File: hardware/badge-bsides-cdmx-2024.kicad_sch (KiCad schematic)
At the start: 26 parts, among them J1 OLED, Q1 DMG3415U-7, SW1 ON, SW2 RESET, SW3 RESET, SW4 RESET, SW5 RESET, SW6 RESET

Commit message: feat(Hw):Added_LED´s_Buttons
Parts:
- D2: value LED1 -> RED; footprint (none) -> LED_SMD:LED_0805_2012Metric; LCSC# (none) -> C965812; provedor (none) -> LCSC
- D3: value LED2 -> Green; footprint (none) -> LED_SMD:LED_0805_2012Metric; LCSC# (none) -> C965815; provedor (none) -> LCSC
- D4: value LED3 -> Blue; footprint (none) -> LED_SMD:LED_0805_2012Metric; LCSC# (none) -> C205441; provedor (none) -> LCSC
- D5: value LED4 -> Yellow; footprint (none) -> LED_SMD:LED_0805_2012Metric; LCSC# (none) -> C84261; provedor (none) -> LCSC
- D6: footprint (none) -> LED_SMD:LED_0805_2012Metric
- J1: value OLED -> Purple; footprint (none) -> LED_SMD:LED_0805_2012Metric; LCSC# (none) -> C7371915
- R2, R3, R4, R5, R6: value 220R -> 330R; footprint (none) -> Resistor_SMD:R_0805_2012Metric_Pad1.20x1.40mm_HandSolder; LCSC# (none) -> C119075; provedor (none) -> LCSC
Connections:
- net RST: now reaches A1.30 (RUN)
- net RST: now also SW5.2
- no-connect marks 0 -> 19

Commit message: fix(Hw):Changed_raspberry
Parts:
- removed A1: SC0918, bsides:MODULE_SC0918, symbol Raspberry_Pi_Pico_W_SC0918:SC0918
- removed BT1: Battery_Cell, symbol Device:Battery_Cell
- removed D3: Green, LED_SMD:LED_0805_2012Metric, symbol Device:LED_Small
- removed D4: Blue, LED_SMD:LED_0805_2012Metric, symbol Device:LED_Small
- removed D5: Yellow, LED_SMD:LED_0805_2012Metric, symbol Device:LED_Small
- removed D6: LED5, LED_SMD:LED_0805_2012Metric, symbol Device:LED_Small
- removed J1: Purple, LED_SMD:LED_0805_2012Metric, symbol Connector:Conn_01x04_Socket
- removed R3, R4, R5, R6: 330R, Resistor_SMD:R_0805_2012Metric_Pad1.20x1.40mm_HandSolder, symbol Device:R_Small
- removed SW5: RESET, Button_Switch_SMD:SW_SPST_TL3342, symbol Switch:SW_Push
- added C5, C6: .1uF, Capacitor_SMD:C_0603_1608Metric, symbol Device:C_Small
- added C8, C9: 10uF, Capacitor_SMD:C_0603_1608Metric, symbol Device:C_Small
- added F1: 0.5A, Fuse:Fuse_0805_2012Metric, symbol Device:Fuse_Small
- added J2: I2C, Connector_PinHeader_2.54mm:PinHeader_1x04_P2.54mm_Vertical, symbol Connector:Screw_Terminal_01x04
- added J3: UART, Connector_PinHeader_2.54mm:PinHeader_1x05_P2.54mm_Vertical, symbol Connector:Screw_Terminal_01x05
- added J4: Battery, Footprint:BAT-TH_BH-AAA-A1AJ024, symbol Connector:Screw_Terminal_01x02
- added J5: OLED, Connector_PinHeader_2.54mm:PinHeader_1x04_P2.54mm_Vertical, symbol Connector:Screw_Terminal_01x04
- added P1: USB_C_Plug_USB2.0, Footprint:C393939, symbol HunterCat-NFC-rescue:USB_C_Plug_USB2.0-Connector
- added R7, R8: 5k1, Resistor_SMD:R_0603_1608Metric, symbol Device:R_Small
- added R9: 10K, Resistor_SMD:R_0603_1608Metric, symbol Device:R_Small
- added SW7: RESET, Button_Switch_SMD:SW_SPST_TL3342, symbol Switch:SW_Push
- added SW8: GPIO, Button_Switch_SMD:SW_SPST_TL3342, symbol Switch:SW_Push
- added U1: ESP32-C6-WROOM-1U-N4, Footprint:MOD28_ESP32-C6-WROOM-1U_EXP, symbol Minino:ESP32-C6-WROOM-1U-N8
- added U2: AP2112K-3.3, Package_TO_SOT_SMD:SOT-23-5, symbol HunterCat-NFC-rescue:AP2112K-3.3-Regulator_Linear
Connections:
- net +BATT: now also J4.2 (Pin_2)
- net GND: now also C5.1, C6.1, C8.2, C9.2, J2.4 (Pin_4), J3.4 (Pin_4), J4.1 (Pin_1), J5.2 (Pin_2), P1.A1 (GND), P1.A12 (GND), P1.B1 (GND), P1.B12 (GND), P1.S1 (SHIELD), R7.1, R8.1, SW7.1, SW8.1, U1.1 (GND), U1.28 (GND), U1.29 (GND), U1.30 (GND), U1.31 (GND), U1.32 (GND), U1.33 (GND), U1.34 (GND), U1.35 (GND), U1.36 (GND), U1.37 (GND), U2.2 (GND)
- net LED1: now also U1.10 (IO8)
- net SCL: now also J2.2 (Pin_2), J5.3 (Pin_3), U1.7 (IO7)
- net SDA: now also J2.3 (Pin_3), J5.4 (Pin_4), U1.6 (IO6)
- net VBUS: now also F1.2
- net GPIO16 renamed GPIO15
- net GPIO15: now also U1.23 (IO15)
- net GPIO17 renamed GPIO23
- net GPIO23: now also U1.21 (IO23)
- net GPIO18 renamed GPIO22
- net GPIO22: now also U1.20 (IO22)
- net GPIO19 renamed GPIO1
- net GPIO1: now also U1.9 (IO1)
- net VCC: no longer names the net of SW1.2 (B)
- net VCC: now also C8.1, U2.1 (VIN), U2.3 (EN)
- new net: P1.A5 (CC), R7.2
- new net: F1.1, P1.A4 (VBUS), P1.A9 (VBUS), P1.B4 (VBUS), P1.B9 (VBUS)
- new net: P1.B5 (VCONN), R8.2
- new net +3V3: C9.1, J2.1 (Pin_1), J3.1 (Pin_1), J5.1 (Pin_1), R9.2, U1.2 (3V3), U2.5 (VOUT)
- new net BOOT: C6.2, SW8.2, U1.15 (IO9)
- new net D+: P1.A6 (D+), U1.14 (IO13)
- new net D-: P1.A7 (D-), U1.13 (IO12)
- new net DIO11: J3.5 (Pin_5)
- new net EN: C5.2, R9.1, SW7.2, U1.3 (EN)
- new net RX: J3.2 (Pin_2), U1.24 (RXD0)
- new net TX: J3.3 (Pin_3), U1.25 (TXD0)
- no-connect marks 19 -> 12
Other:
- moved on the sheet: C1, C2, C3, C4, D2, R2, SW2, SW3, SW4, SW6

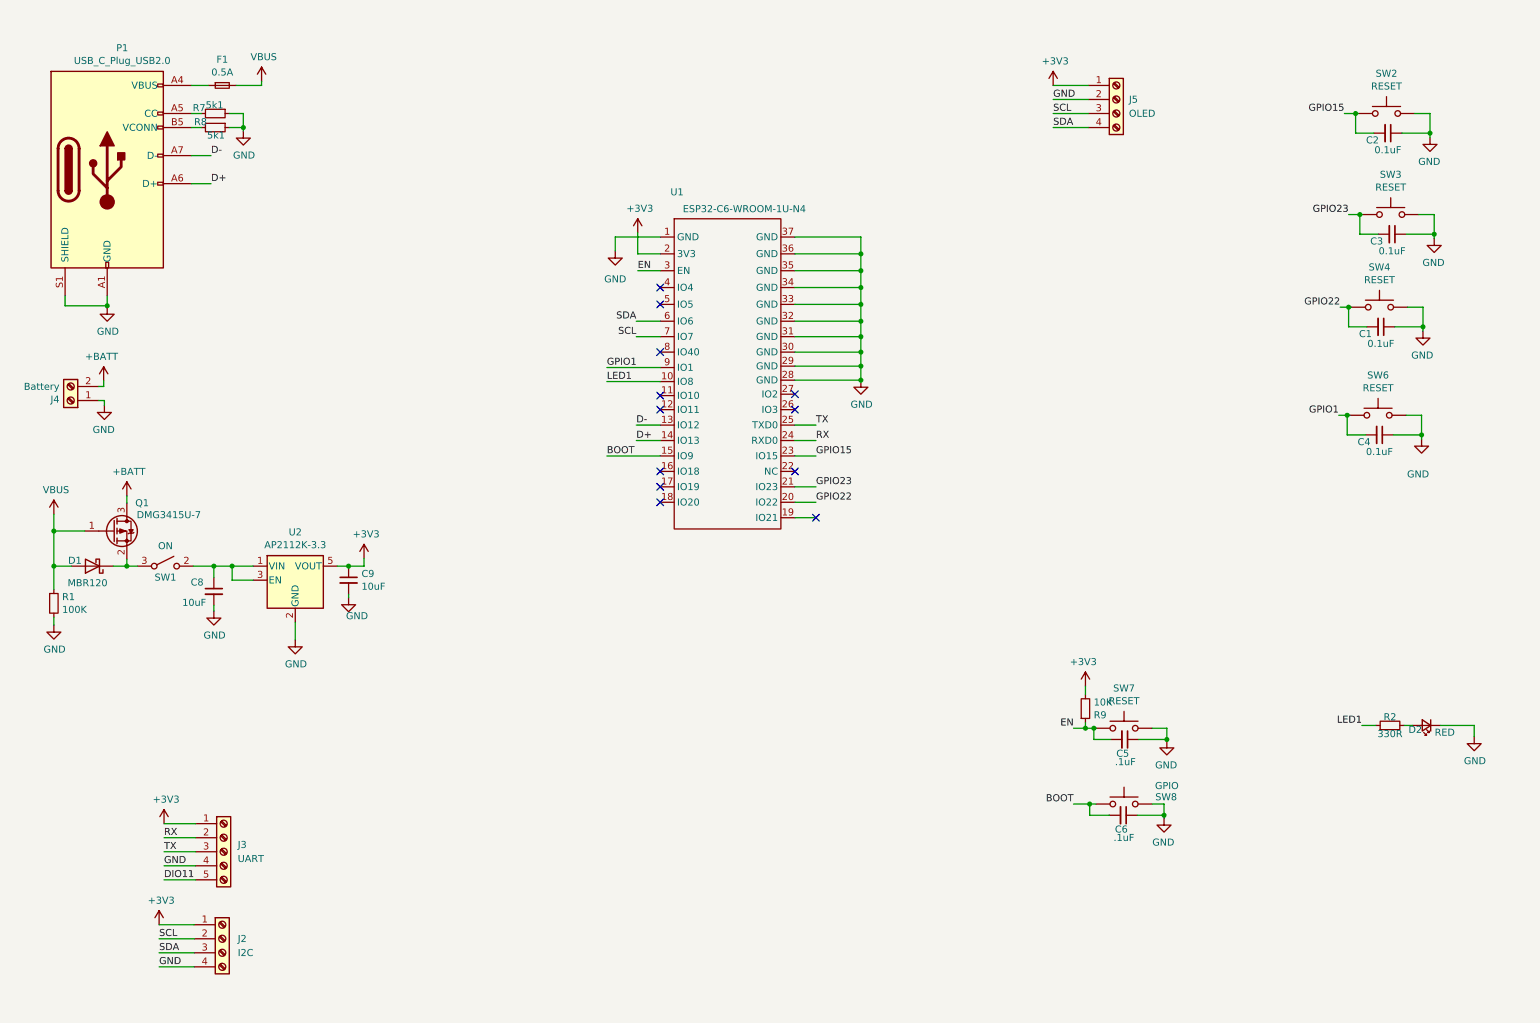
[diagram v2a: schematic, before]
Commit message: feat(hw): add labels schematic
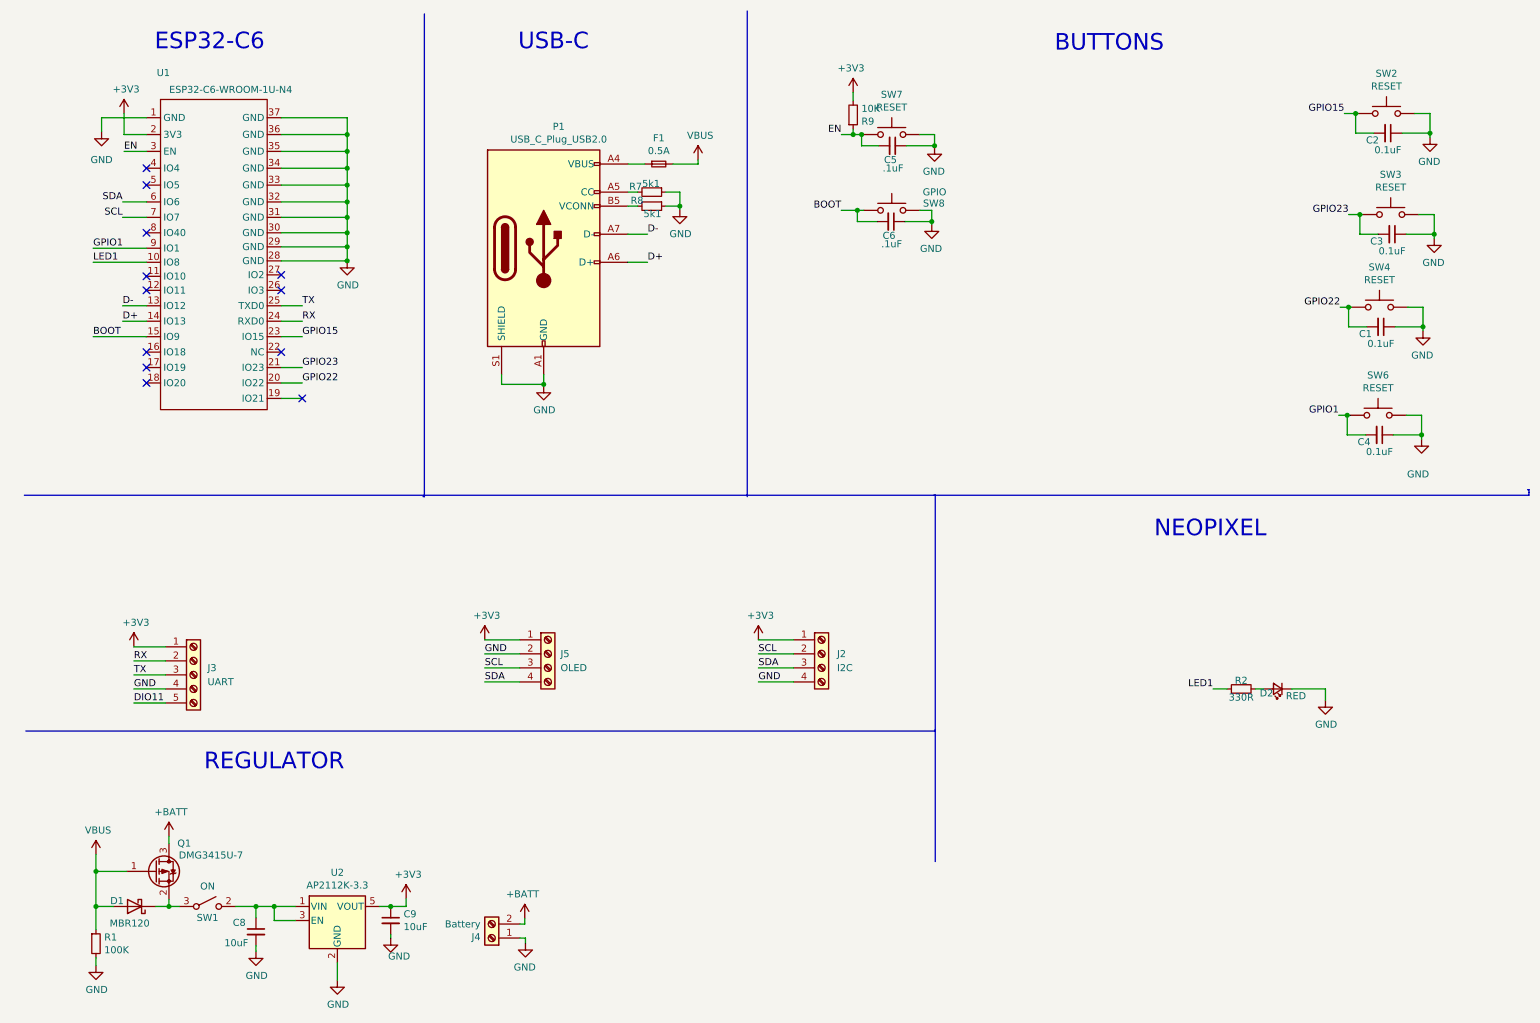
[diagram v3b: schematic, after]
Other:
- note added: "BUTTONS"
- note added: "ESP32-C6"
- note added: "NEOPIXEL"
- note added: "REGULATOR"
- note added: "USB-C"
- moved on the sheet: C5, C6, C8, C9, D1, D2, F1, J2, J3, J4, J5, P1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
